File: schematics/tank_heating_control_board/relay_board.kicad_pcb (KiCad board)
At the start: 2 copper layers, 45 x 75 mm, 51 parts, among them J1 Programming Header, P1 ACT_PWR, P2 ACT_PWR, P3 ACTUATOR, Q1 MMBF170, Q2 MMBF170, SW1 SW_DIP_x04, U1 SPST_POWER_RELAY, U2 PIC16F1826-ISO, U3 dpdt_relay, U4 INA180A1, U5 CONN_01x05, U6 INA180A1, U7 CONN_01x05

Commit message: routed
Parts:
- removed ? (x4): MountingHole_3.2mm_M3_Pad, MountingHole:MountingHole_3.2mm_M3_Pad
- removed C4: 0.1uF, Capacitor_SMD:C_0805_2012Metric_Pad1.18x1.45mm_HandSolder
- removed D5: BLUE 3.2V 10mA, LED_SMD:LED_1206_3216Metric_Pad1.42x1.75mm_HandSolder
- removed D6, D7: D, Diode_SMD:D_SMB_Handsoldering
- removed the G*** at (146.6, 132.0)
- removed P1, P2: ACT_PWR, TerminalBlock_Phoenix:TerminalBlock_Phoenix_MKDS-1,5-2-5.08_1x02_P5.08mm_Horizontal
- removed P3: ACTUATOR, TerminalBlock_Phoenix:TerminalBlock_Phoenix_MKDS-1,5-6_1x06_P5.00mm_Horizontal
- removed Q2: MMBF170, Package_TO_SOT_SMD:SOT-23_Handsoldering
- removed TP0: TEST_1P, custom:Socket_Strip_Straight_1x01_Pitch2.54mm
- removed U5, U7: CONN_01x05, Connector_JST:JST_XH_S5B-XH-A-1_1x05_P2.50mm_Horizontal
- removed U6: INA180A1, Package_TO_SOT_SMD:SOT-23-5_HandSoldering
- added G***: LOGO, custom:rocketry_logo_small, F.Cu at (162.0, 135.2)
- added J2: Power IN from battery, custom:CONN_1714955_PXC, F.Cu at (156.2, 74.7)
- added J3: Power OUT to heater, custom:CONN_1714955_PXC, F.Cu at (142.3, 74.7)
- added J4: Vsense and Thermistor, TerminalBlock_Phoenix:TerminalBlock_Phoenix_PT-1,5-4-5.0-H_1x04_P5.00mm_Horizontal, F.Cu at (175.4, 128.2)
- added K1: AZ2150-1AE-24DEF, custom:AZ2150_AMZ, F.Cu at (160.3, 118.3)
- added R17: 60.4K 1%, Resistor_SMD:R_0805_2012Metric_Pad1.20x1.40mm_HandSolder, B.Cu at (170.5, 118.2)
- added R18: 10K 1%, Resistor_SMD:R_0805_2012Metric_Pad1.20x1.40mm_HandSolder, B.Cu at (166.4, 119.4)
- added REF**: MountingHole_3.2mm_M3_Pad, MountingHole:MountingHole_3.2mm_M3_Pad, F.Cu at (171.1, 138.9)
- added REF**: MountingHole_3.2mm_M3_Pad, MountingHole:MountingHole_3.2mm_M3_Pad, F.Cu at (134.0, 73.9)
- added REF**: MountingHole_3.2mm_M3_Pad, MountingHole:MountingHole_3.2mm_M3_Pad, F.Cu at (134.1, 138.9)
- added REF**: MountingHole_3.2mm_M3_Pad, MountingHole:MountingHole_3.2mm_M3_Pad, F.Cu at (171.1, 73.9)
- C3, R2, R3, R4, U4: moved to F.Cu
- D1: value D -> BLUE 3.2V 10mA; footprint Diode_SMD:D_SMB_Handsoldering -> LED_SMD:LED_1206_3216Metric_Pad1.42x1.75mm_HandSolder; moved to F.Cu
- D2: value D -> STPS2L25U
- D3: value D -> RED; footprint Diode_SMD:D_SMB_Handsoldering -> LED_SMD:LED_1206_3216Metric_Pad1.42x1.75mm_HandSolder; moved to F.Cu
- D4: value D -> GREEN; footprint Diode_SMD:D_SMB_Handsoldering -> LED_SMD:LED_1206_3216Metric_Pad1.42x1.75mm_HandSolder; moved to F.Cu
- F1: value FUSE -> 30A; footprint custom:littlefuse_01000020Z -> custom:3557-10_KEY
- J1: value Programming Header -> Conn_01x05_Socket; moved to F.Cu
- Q1: footprint Package_TO_SOT_SMD:SOT-23_Handsoldering -> Package_TO_SOT_SMD:SOT-23
- R1: value 10k -> 10K; moved to F.Cu
- R10: value 10K -> 150
- R12, R13: value 10K -> 2.2K; moved to F.Cu
- R14: value 0.01 -> TBD; footprint Resistor_SMD:R_2512_6332Metric_Pad1.40x3.35mm_HandSolder -> Resistor_SMD:R_0805_2012Metric_Pad1.20x1.40mm_HandSolder; moved to B.Cu
- R15: value 0.01 -> 60.4K 1%; footprint Resistor_SMD:R_2512_6332Metric_Pad1.40x3.35mm_HandSolder -> Resistor_SMD:R_0805_2012Metric_Pad1.20x1.40mm_HandSolder; moved to B.Cu
- R16: value 180 -> 10K 1%; moved to B.Cu
- R5: value 150 -> 10k; moved to F.Cu
- R6: value 150 -> 180; moved to F.Cu
- R7: value 20K -> 60.4K 1%; moved to F.Cu
- R8: value 10K -> 10K 1%
- R9: value 20K -> 0.001 1%; footprint Resistor_SMD:R_0805_2012Metric_Pad1.20x1.40mm_HandSolder -> Resistor_SMD:R_2512_6332Metric_Pad1.40x3.35mm_HandSolder; moved to F.Cu
- U1: value SPST_POWER_RELAY -> JST I2C Connector; footprint custom:Relay_SPST_G5LE-1A -> Connector_JST:JST_XH_S5B-XH-A-1_1x05_P2.50mm_Horizontal
- U2: value PIC16F1826-ISO -> JST I2C Connector; footprint custom:PIC16F1826-ISO -> Connector_JST:JST_XH_S5B-XH-A-1_1x05_P2.50mm_Horizontal; moved to F.Cu
- U3: value dpdt_relay -> PIC16F1826-ISO; footprint custom:Relay_DPDT_RT424012F -> custom:PIC16F1826-ISO; moved to B.Cu
- moved R14 69.3 mm to (179.3, 133.6), turned to -90 degrees
- moved SW1 64.6 mm to (172.3, 80.0), turned to 0 degrees
- moved R8 62.2 mm to (140.9, 136.9), turned to 180 degrees
- moved D3 61.3 mm to (178.7, 134.1)
- moved D1 58.3 mm to (176.2, 140.0), turned to 90 degrees
- moved R7 56.1 mm to (170.5, 133.2)
- moved TP3 51.0 mm to (132.6, 123.6), turned to 0 degrees
- moved R10 49.5 mm to (135.9, 116.8), turned to 90 degrees
- moved R2 48.7 mm to (172.2, 91.9)
- moved R3 48.3 mm to (174.8, 91.8)
- moved R4 48.2 mm to (177.3, 91.9)
- moved C2 47.3 mm to (151.4, 137.5), turned to 180 degrees
- moved R11 41.5 mm to (133.0, 116.8), turned to 90 degrees
- moved R15 41.3 mm to (170.6, 113.2)
- moved R6 41.1 mm to (179.3, 140.5), turned to 90 degrees
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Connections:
- D1 pad 1: +12V -> Net-(D1-K)
- D1 pad 2: Net-(D1-Pad2) -> Net-(D1-A)
- D2 pad 1: +12V -> +24V
- D2 pad 2: Net-(D2-Pad2) -> Net-(D2-A)
- D3 pad 1: /G1 -> GND
- D3 pad 2: GND -> Net-(D3-A)
- D4 pad 1: /G2 -> GND
- D4 pad 2: GND -> Net-(D4-A)
- F1 pad 1: Net-(F1-Pad1) -> +24V
- F1 pad 2: Net-(F1-Pad2) -> Net-(J2-Pin_1)
- J1 pad 1: /ICSPCLK -> /~{MCLR}
- J1 pad 2: /ICSPDAT -> +5V
- J1 pad 4: +5V -> /ICSPDAT
- J1 pad 5: /~{MCLR} -> /ICSPCLK
- Q1 pad 1: Net-(Q1-Pad1) -> Net-(Q1-G)
- Q1 pad 3: Net-(D1-Pad2) -> Net-(D2-A)
- R1 pad 2: /DIP_1 -> /~{MCLR}
- R10 pad 1: /LIM2 -> Net-(Q1-G)
- R10 pad 2: GND -> /PWR_CTRL
- R11 pad 1: Net-(Q1-Pad1) -> Net-(Q1-G)
- R12 pad 1: Net-(Q2-Pad1) -> +24V
- R12 pad 2: GND -> Net-(D3-A)
- R13 pad 1: +5V -> /PWR_OUT
- R13 pad 2: /~{MCLR} -> Net-(D4-A)
- R14 pad 1: /P1 -> /THERMISTOR
- R14 pad 2: Net-(R14-Pad2) -> GND
- R15 pad 1: /P2 -> Net-(J4-Pin_4)
- R15 pad 2: Net-(R15-Pad2) -> /HEATER_VSENSE_P
- R16 pad 1: Net-(D5-Pad1) -> /HEATER_VSENSE_P
- R2 pad 2: /DIP_2 -> /DIP_1
- R3 pad 2: /DIP_3 -> /DIP_2
- R4 pad 2: /DIP_4 -> /DIP_3
- R5 pad 1: Net-(Q1-Pad1) -> +5V
- R5 pad 2: /POWER -> /DIP_4
- R6 pad 1: Net-(Q2-Pad1) -> Net-(D1-K)
- R6 pad 2: /SELECT -> GND
- R7 pad 1: Net-(P3-Pad2) -> +24V
- R7 pad 2: /LIM1 -> /24VSENSE
- R8 pad 1: /LIM1 -> /24VSENSE
- R9 pad 1: Net-(P3-Pad1) -> Net-(J3-Pin_1)
- R9 pad 2: /LIM2 -> /PWR_OUT
- TP1 pad 1: +12V -> GND
- TP2 pad 1: +5V -> +24V
- TP3 pad 1: Net-(F1-Pad2) -> +5V
- U1 pad 1: +12V -> Net-(U1-Pad1)
- U1 pad 2: Net-(D1-Pad2) -> +5V
- U1 pad 3: Net-(F1-Pad2) -> GND
- U1 pad 4: Net-(U1-Pad4) -> /SCL
- U2 pad 1: /POWER -> /SDA
- U2 pad 2: /SELECT -> /SCL
- U2 pad 3: /DIP_1 -> GND
- U2 pad 4: /~{MCLR} -> +5V
- U2 pad 5: GND -> Net-(U1-Pad1)
- U3 pad 1: Net-(U1-Pad4) -> /PWR_CTRL
- U3 pad 2: GND -> /THERMISTOR
- U3 pad 3: Net-(D2-Pad2) -> /DIP_1
- U3 pad 4: +12V -> /~{MCLR}
- U3 pad 5: Net-(R14-Pad2) -> GND
- U3 pad 6: Net-(R15-Pad2) -> /DIP_2
- U3 pad 7: /G1 -> /SDA
- U3 pad 8: /G2 -> /DIP_3
- U4 pad 1: /CURR_SENSE_1 -> /CURR_SENSE
- U4 pad 3: Net-(R14-Pad2) -> /PWR_OUT
- U4 pad 4: /P1 -> Net-(J3-Pin_1)
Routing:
- net +5V: track 172.8 -> 8.35 mm, vias 5 -> 1
- net GND: track 175.7 -> 36.0 mm, vias 11 -> 10
- net +12V: track 120.1 -> 0.00 mm, vias 1 -> 0
- net /CURR_SENSE: track 0.00 -> 54.3 mm, vias 0 -> 1
- net /THERMISTOR: track 0.00 -> 53.5 mm, vias 0 -> 2
- net /LIM2: track 45.5 -> 0.00 mm
- net /DIP_1: track 41.8 -> 84.6 mm, vias 3 -> 0
- net /LIM1: track 42.6 -> 0.00 mm
- net Net-(F1-Pad1): track 42.6 -> 0.00 mm
- net /SDA: track 39.5 -> 81.8 mm, vias 1 -> 2
- net /DIP_2: track 33.7 -> 75.8 mm
- net /SCL: track 44.7 -> 85.7 mm, vias 0 -> 2
- net /24VSENSE: track 0.00 -> 41.0 mm, vias 0 -> 1
- net Net-(U1-Pad1): track 0.00 -> 40.5 mm
- net /HEATER_VSENSE_P: track 0.00 -> 39.8 mm
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- added copper zone on F.Cu, net +24V
- added copper zone on F.Cu, net +5V
- added copper zone on F.Cu, net /PWR_OUT
- added copper zone on F.Cu, net Net-(J2-Pin_1)
- added copper zone on F.Cu, net Net-(J3-Pin_1)
- removed copper zone on F.Cu, net GND
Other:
- board size 45 x 75 mm -> 51.7 x 75 mm
- board text added: "{dblquote}Bloor Dundas-West Station{dblquote} Tank Heating Control Board Jason Xu R1 June 2024"
- board text removed: "0"
- board text removed: "1"
- board text removed: "12V"
- board text removed: "12V 5V GND SCL SDA"
- board text removed: "2"
- board text removed: "3"
- board text removed: "4"
- board text removed: "5V"
- board text removed: "ACT_PWR"
- board text removed: "G1"
- board text removed: "G2"
- board text removed: "GND"
- board text removed: "L1"
- board text removed: "L2"
- board text removed: "PWR"
- board text removed: "RLCS Relay Board"
- board text removed: "SDA SCL GND 5V 12V"
- board text removed: "V1"
- board text removed: "V2"
- board text removed: "~{MCLR} 5V"

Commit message: Change current sense to low side
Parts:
- C3, R9, U4: moved to B.Cu
- moved U4 8.19 mm to (142.5, 80.7), turned to -90 degrees
- moved R9 7.35 mm to (148.6, 81.1), turned to 90 degrees
- moved C3 5.82 mm to (141.5, 85.8), turned to 90 degrees
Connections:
- net Net-(U1-Pad1) renamed +12V
- J3 pad 1: Net-(J3-Pin_1) -> /PWR_OUT
- J3 pad 2: GND -> Net-(J3-Pin_2)
- R9 pad 1: Net-(J3-Pin_1) -> GND
- R9 pad 2: /PWR_OUT -> Net-(J3-Pin_2)
- U4 pad 3: /PWR_OUT -> Net-(J3-Pin_2)
- U4 pad 4: Net-(J3-Pin_1) -> GND
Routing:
- net /CURR_SENSE: track 54.3 -> 66.1 mm, vias 1 -> 2
- net +5V: track 8.35 -> 15.2 mm, vias 1 -> 2
- net GND: track 36.0 -> 29.5 mm, vias 10 -> 9
- net Net-(J3-Pin_2): track 0.00 -> 2.05 mm
- net /SDA: track 81.8 -> 81.0 mm
- added copper zone on B.Cu, net Net-(J3-Pin_2)
- removed copper zone on F.Cu, net Net-(J3-Pin_1)

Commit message: Specify JLC part number location
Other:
- board text added: "JLCJLCJLCJLC"
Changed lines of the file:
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@@
 		(tags "resistor handsolder")
 		(property "Reference" "R9"
-			(at 0 2.62 270)
+			(at 0 2.62 -90)
 			(layer "B.SilkS")
 			(effects
@@
 		)
 		(property "Value" "0.001 1%"
-			(at 0 -2.62 270)
+			(at 0 -2.62 -90)
 			(layer "B.Fab")
 			(effects
@@
 		)
 		(fp_text user "${REFERENCE}"
-			(at 0 0 270)
+			(at 0 0 -90)
 			(layer "B.Fab")
 			(effects
@@
 		(tags "capacitor handsolder")
 		(property "Reference" "C3"
-			(at 0 1.68 270)
+			(at 0 1.68 -90)
 			(layer "B.SilkS")
 			(effects
@@
 		)
 		(property "Value" "0.1uF"
-			(at 0 -1.68 270)
+			(at 0 -1.68 -90)
 			(layer "B.Fab")
 			(effects
@@
 		)
 		(fp_text user "${REFERENCE}"
-			(at 0 0 270)
+			(at 0 0 -90)
 			(layer "B.Fab")
 			(effects
@@
 				(bold yes)
 			)
+			(justify left bottom)
+		)
+	)
+	(gr_text "JLCJLCJLCJLC"
+		(at 154.432 116.1796 90)
+		(layer "F.SilkS")
+		(effects
+			(font
+				(size 1.5 1.5)
+				(thickness 0.3)
+				(bold yes)
+			)

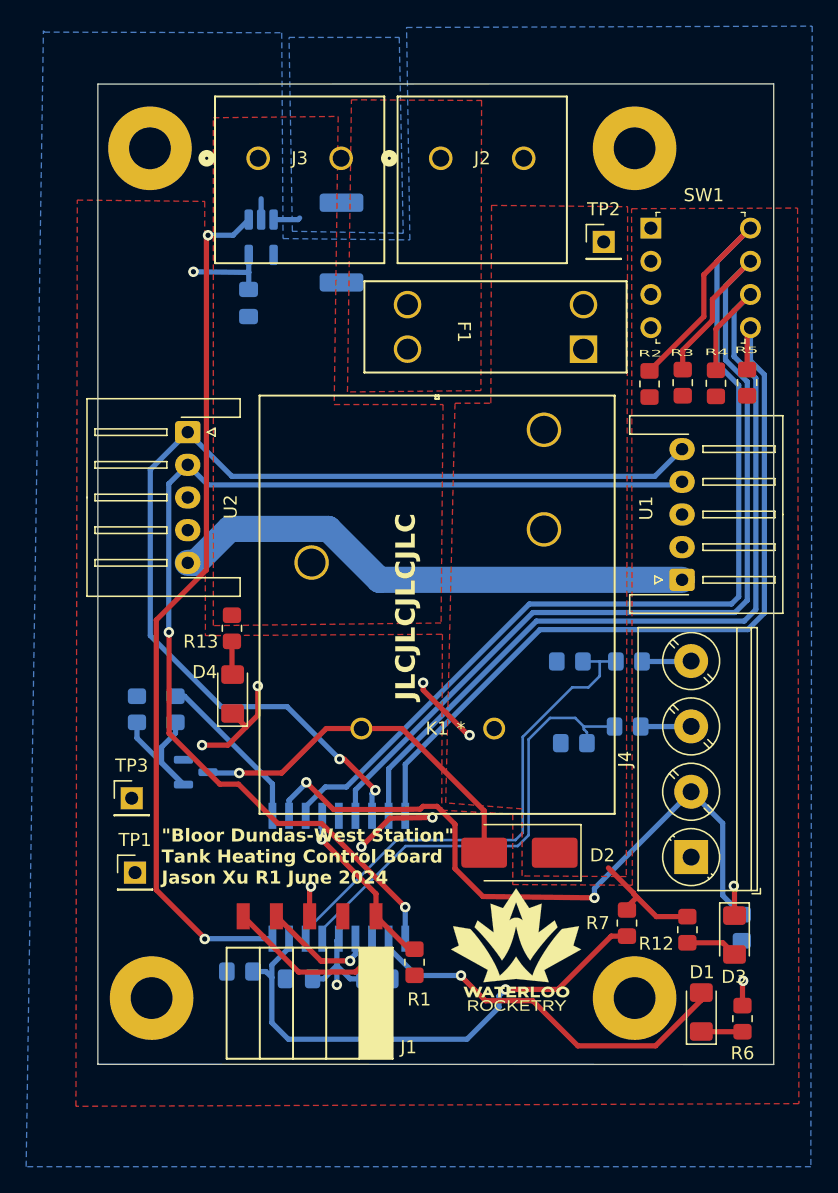
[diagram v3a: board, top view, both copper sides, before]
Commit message: Fix silkscreen
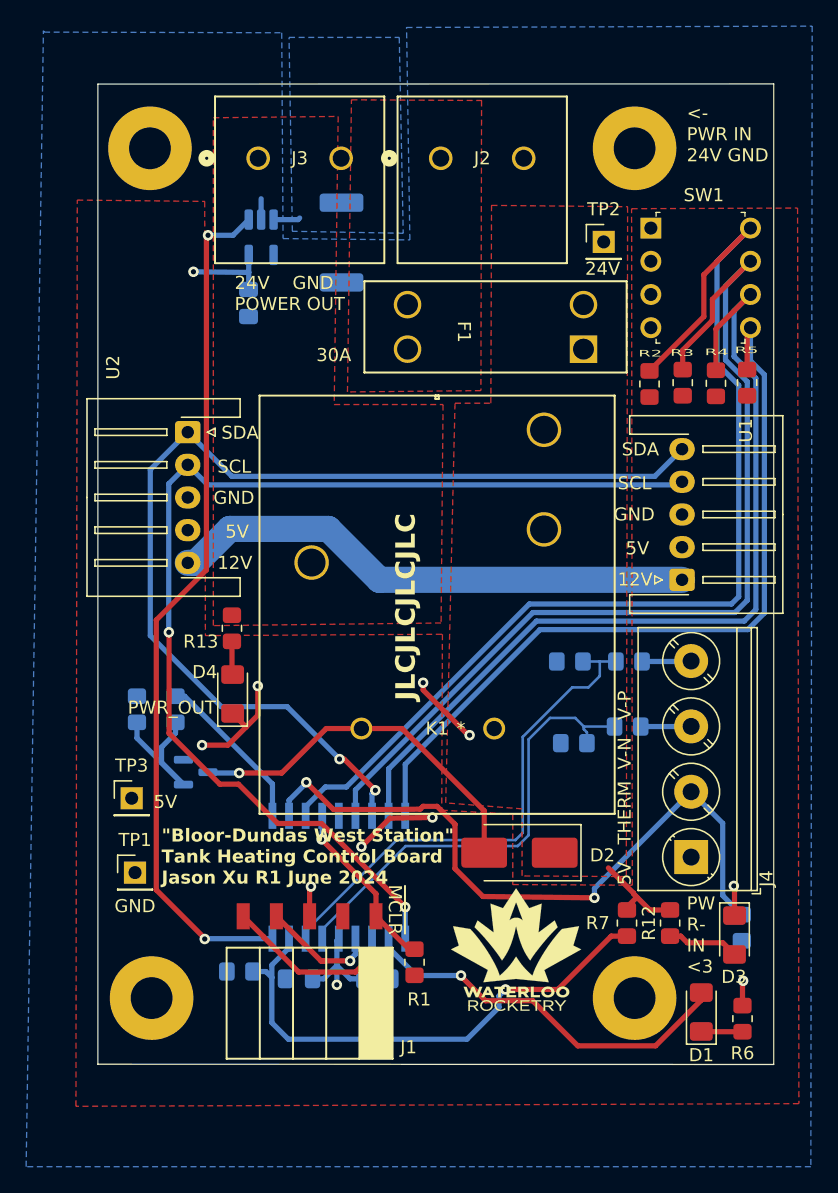
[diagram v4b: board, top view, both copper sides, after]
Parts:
- moved R12 1.42 mm to (173.8, 133.2)
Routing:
- net +24V: track 8.91 -> 7.38 mm
- net Net-(D3-A): track 3.98 -> 5.51 mm
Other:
- board text added: "12V"
- board text added: "24V"
- board text added: "24V GND POWER OUT"
- board text added: "30A"
- board text added: "5V"
- board text added: "5V THERM V-N V-P"
- board text added: "<- PWR IN 24V GND"
- board text added: "GND"
- board text added: "PW R- IN <3"
- board text added: "PWR_OUT"
- board text added: "SCL"
- board text added: "SDA"
- board text added: "{dblquote}Bloor-Dundas West Station{dblquote} Tank Heating Control Board Jason Xu R1 June 2024"
- board text added: "~{MCLR}"
- board text removed: "{dblquote}Bloor Dundas-West Station{dblquote} Tank Heating Control Board Jason Xu R1 June 2024"

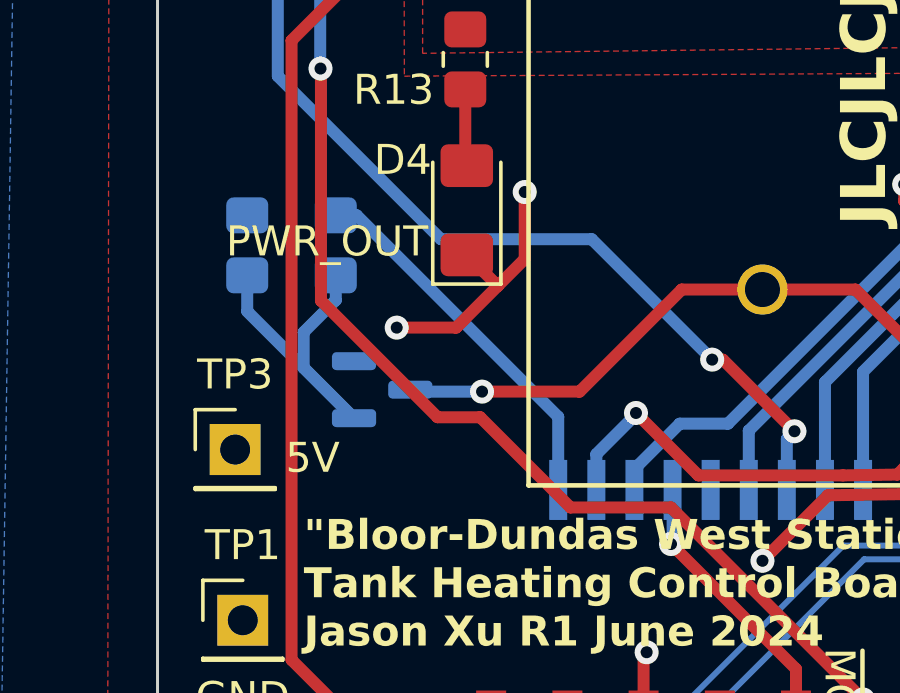
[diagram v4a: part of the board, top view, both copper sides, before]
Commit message: Fix ground and add gerber
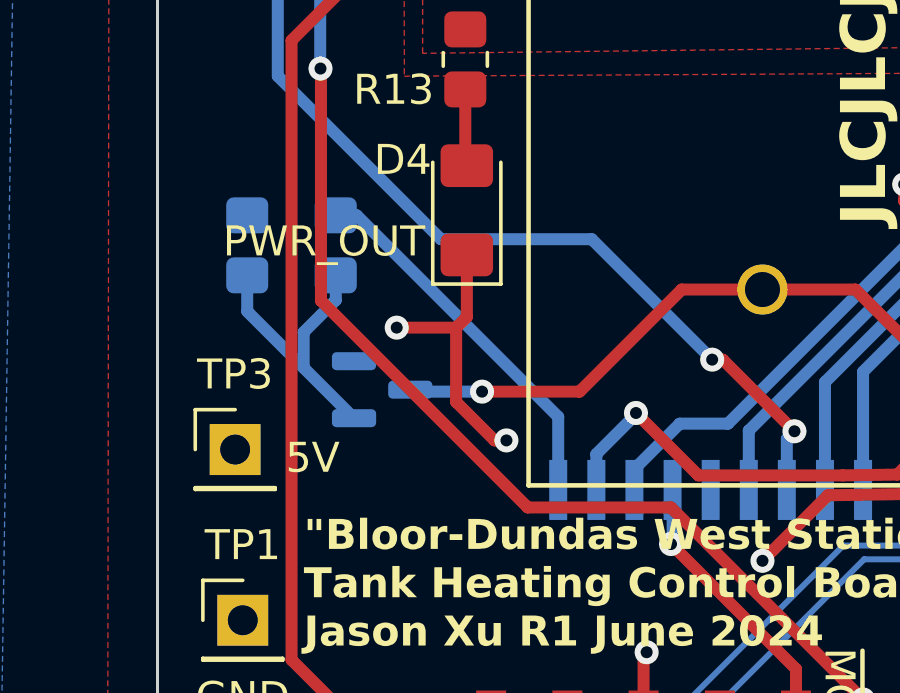
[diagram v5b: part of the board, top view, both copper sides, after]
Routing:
- net Net-(Q1-G): track 12.1 -> 9.76 mm
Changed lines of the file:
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@@
 		(allow_soldermask_bridges_in_footprints no)
 		(pcbplotparams
-			(layerselection 0x00010f0_ffffffff)
+			(layerselection 0x00010fc_ffffffff)
 			(plot_on_all_layers_selection 0x0000000_00000000)
 			(disableapertmacros no)
@@
 			(plotinvisibletext no)
 			(sketchpadsonfab no)
-			(subtractmaskfromsilk no)
+			(subtractmaskfromsilk yes)
 			(outputformat 1)
 			(mirror no)
 			(drillshape 0)
 			(scaleselection 1)
-			(outputdirectory "../../gerbers/relay_board_v2_gerbers/")
+			(outputdirectory "../../gerbers/heating_control_gerbers/")
 		)
 	)
@@
 	)
 	(gr_text "PWR_OUT"
-		(at 132.2832 117.2972 0)
+		(at 132.1816 117.2972 0)
 		(layer "F.SilkS")
 		(effects
@@
 	)
 	(segment
-		(start 142.24 115.062)
-		(end 142.24 117.2972)
-		(width 0.4)
-		(layer "F.Cu")
-		(net 1)
-	)
-	(segment
 		(start 146.2024 130.5052)
 		(end 146.304 130.4036)
@@
 	)
 	(segment
-		(start 141.34385 118.19335)
-		(end 140.3096 117.1591)
+		(start 141.6304 123.3424)
+		(end 141.235461 123.3424)
 		(width 0.4)
 		(layer "F.Cu")
@@
 	)
 	(segment
-		(start 142.24 117.2972)
-		(end 141.34385 118.19335)
-		(width 0.4)
-		(layer "F.Cu")
-		(net 1)
-	)
-	(segment
 		(start 146.177 130.5306)
 		(end 146.304 130.4036)
@@
 	(segment
 		(start 139.954 119.5832)
-		(end 141.34385 118.19335)
+		(end 140.3096 119.2276)
 		(width 0.4)
 		(layer "F.Cu")
@@
 	)
 	(segment
+		(start 141.235461 123.3424)
+		(end 139.954 122.060939)
+		(width 0.4)
+		(layer "F.Cu")
+		(net 1)
+	)
+	(segment
 		(start 154.8892 114.808)
 		(end 154.8892 115.3668)
@@
 	)
 	(segment
+		(start 139.954 122.060939)
+		(end 139.954 119.5832)
+		(width 0.4)
+		(layer "F.Cu")
+		(net 1)
+	)
+	(segment
 		(start 158.4452 118.8212)
 		(end 158.4452 118.9228)
@@
 	)
 	(segment
+		(start 140.3096 119.2276)
+		(end 140.3096 117.1591)
+		(width 0.4)
+		(layer "F.Cu")
+		(net 1)
+	)
+	(segment
 		(start 150.1648 127.3556)
 		(end 152.3492 125.1712)
@@
 	)
 	(via
-		(at 137.9728 119.5832)
+		(at 141.6304 123.3424)
 		(size 0.8)
 		(drill 0.4)
@@
 	)
 	(via
-		(at 146.304 130.4036)
+		(at 137.9728 119.5832)
 		(size 0.8)
 		(drill 0.4)
@@
 	)
 	(via
-		(at 178.6636 130.3528)
+		(at 146.304 130.4036)
 		(size 0.8)
 		(drill 0.4)
@@
 	)
 	(via
-		(at 158.4452 118.8212)
+		(at 178.6636 130.3528)
 		(size 0.8)
 		(drill 0.4)
 		(layers "F.Cu" "B.Cu")
+		(free yes)
 		(net 1)
 	)
 	(via
-		(at 154.8892 114.808)
+		(at 158.4452 118.8212)
 		(size 0.8)
 		(drill 0.4)
 		(layers "F.Cu" "B.Cu")
-		(free yes)
 		(net 1)
 	)
 	(via
-		(at 142.24 115.062)
+		(at 154.8892 114.808)
 		(size 0.8)
 		(drill 0.4)
@@
 	)
 	(segment
-		(start 142.24 115.1128)
-		(end 142.2908 115.1636)
-		(width 0.4)
-		(layer "B.Cu")
-		(net 1)
-	)
-	(segment
-		(start 142.24 115.062)
-		(end 142.24 115.1128)
-		(width 0.4)
-		(layer "B.Cu")
-		(net 1)
-	)
-	(segment
 		(start 142.494 79.3712)
 		(end 142.494 77.7748)
@@
 	)
 	(segment
-		(start 136.5504 122.6008)
-		(end 134.874 120.9244)
-		(width 0.4)
-		(layer "B.Cu")
-		(net 18)
-	)
-	(segment
 		(start 134.874 119.7356)
 		(end 135.9408 118.6688)
@@
 	)
 	(segment
-		(start 135.4474 118.6834)
-		(end 135.4474 110.9618)
-		(width 0.4)
-		(layer "F.Cu")
-		(net 26)
-	)
-	(segment
-		(start 135.4474 110.9618)
-		(end 135.4328 110.9472)
-		(width 0.4)
-		(layer "F.Cu")
-		(net 26)
-	)
-	(segment
-		(start 140.7572 122.5708)
-		(end 139.3348 122.5708)
+		(start 153.5176 131.9784)
+		(end 147.1168 125.5776)
 		(width 0.4)
 		(layer "F.Cu")
@@
 	)
 	(segment
-		(start 139.3348 122.5708)
+		(start 142.3416 125.5776)
 		(end 135.4474 118.6834)
 		(width 0.4)
@@
 	)
 	(segment
-		(start 143.764 125.5776)
-		(end 140.7572 122.5708)
+		(start 147.1168 125.5776)
+		(end 142.3416 125.5776)
 		(width 0.4)
 		(layer "F.Cu")
@@
 	)
 	(segment
-		(start 147.1168 125.5776)
-		(end 143.764 125.5776)
+		(start 135.4474 118.6834)
+		(end 135.4474 110.9618)
 		(width 0.4)
 		(layer "F.Cu")
@@
 	)
 	(segment
-		(start 153.5176 131.9784)
-		(end 147.1168 125.5776)
+		(start 135.4474 110.9618)
+		(end 135.4328 110.9472)
 		(width 0.4)
 		(layer "F.Cu")
